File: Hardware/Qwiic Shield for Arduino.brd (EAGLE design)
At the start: 53.3 x 59.7 mm, 25 parts, among them J1 Qwiic Right Angle, J10 Qwiic Right Angle, J8 Qwiic Right Angle, J9 Qwiic Right Angle, Q1 BSS138, Q2 BSS138, U1 ARDUINO UNO

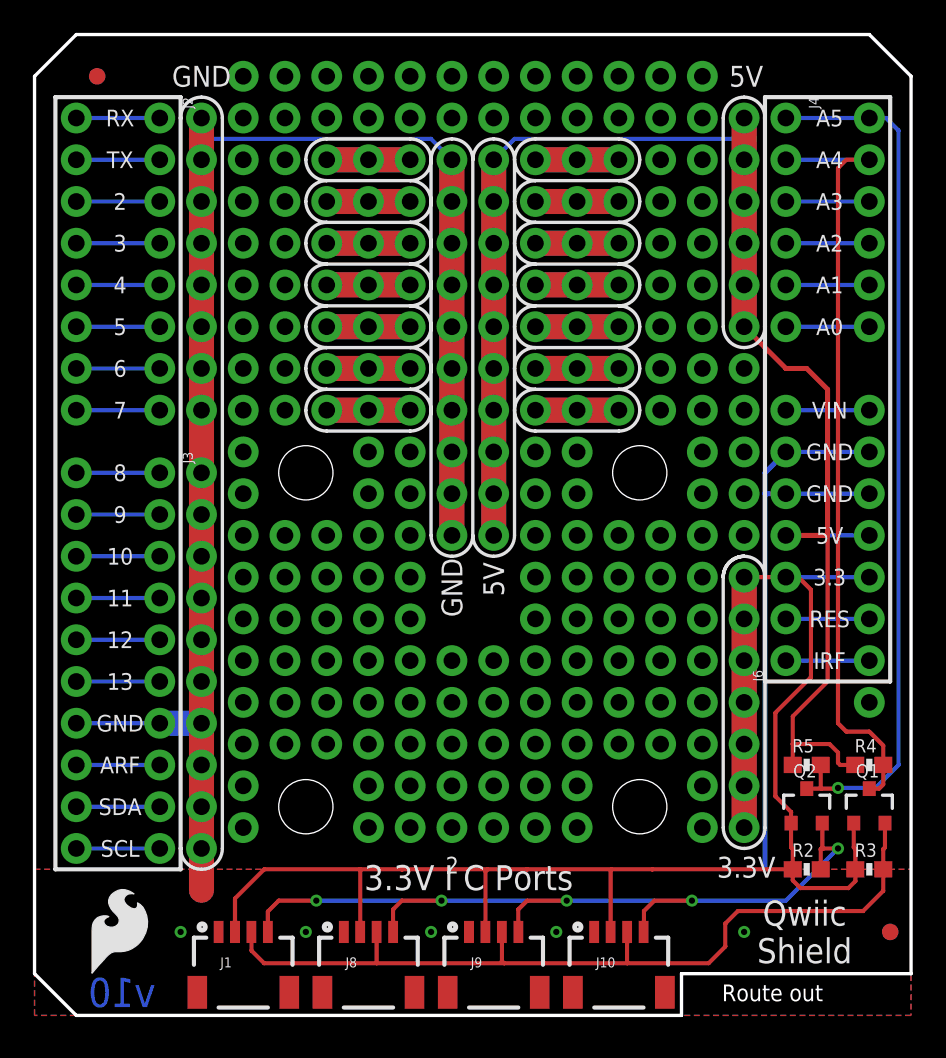
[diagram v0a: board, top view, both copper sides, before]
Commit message: Connected R3 SDA/SCL pins and IOREF
-SDA and SCL are now connected to both A4 /A5 pins and SDA/SCL pins.
-Changed "high" logic side of converters to IOREF, to allow the Arduino to supply it's own IOREF. This will allow the shield to work with 3.3V logic Arduinos.
-named PTH headers in the row of 3.3V to avoid overlap DRC errors.
bumped version to v11 insch and brd
- Added I2C pullup jumper to bottom side with label
- rerouted SDA/SCL to allow for better GND return in pour
- bumped up 3.3V traces to 0.020 inch for qwiic connectors
- all labels to buzzrds and included qwiic logo
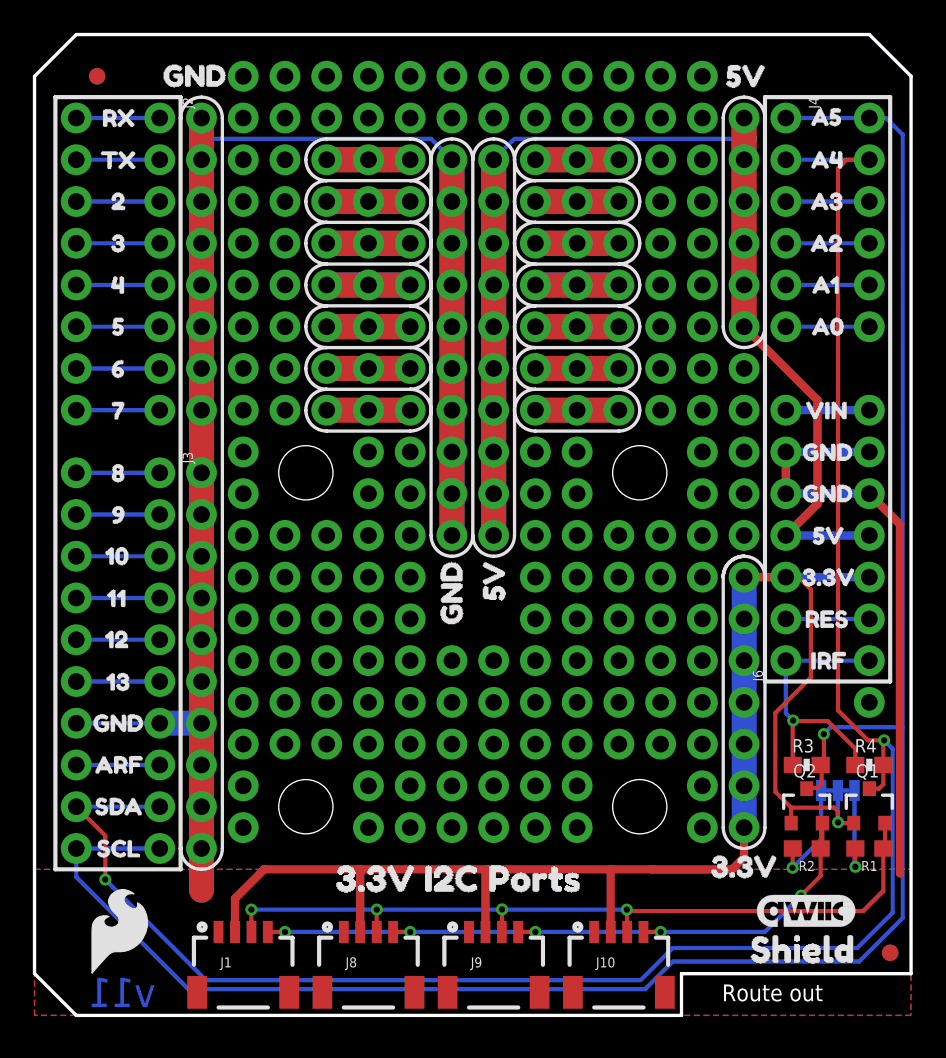
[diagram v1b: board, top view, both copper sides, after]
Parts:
- removed R5: 4.7K, SparkFun-Resistors:0603-RES
- added I2C: (no value), SparkFun-Jumpers:SMT-JUMPER_3_2-NC_TRACE_SILK
- added LOGO3, LOGO4: QWIIC_LOGO_6MM, SparkFun-Aesthetics:QWIIC_6MM
- added R1: 4.7k, SparkFun-Resistors:0603
- added U$10, U$9: (no value), buzzard_labels:TX6
- added U$11, U$12: (no value), buzzard_labels:27
- added U$13, U$14: (no value), buzzard_labels:38
- added U$15, U$16: (no value), buzzard_labels:49
- added U$17, U$18: (no value), buzzard_labels:510
- added U$19, U$20: (no value), buzzard_labels:611
- added U$21, U$23: (no value), buzzard_labels:712
- added U$22: (no value), buzzard_labels (3):I2C0
- added U$24, U$25: (no value), buzzard_labels:813
- added U$26, U$27: (no value), buzzard_labels:914
- added U$28, U$29: (no value), buzzard_labels:1015
- added U$30, U$31: (no value), buzzard_labels:1116
- added U$32, U$33: (no value), buzzard_labels:1217
- added U$34, U$35: (no value), buzzard_labels:1318
- added U$36, U$37, U$68, U$69, U$70, U$71: (no value), buzzard_labels:GND30
- added U$38, U$39: (no value), buzzard_labels:ARF20
- added U$4, U$5: (no value), buzzard_labels:SHIELD0
- added U$40, U$41: (no value), buzzard_labels:SDA21
- added U$42, U$43: (no value), buzzard_labels:SCL22
- added U$44, U$45, U$46, U$47: (no value), buzzard_labels:GND2
- added U$48, U$49: (no value), buzzard_labels:3#3V4
- added U$50, U$51, U$52, U$53: (no value), buzzard_labels:5V3
- added U$54, U$55: (no value), buzzard_labels:A523
- added U$56, U$57: (no value), buzzard_labels:A424
- added U$58, U$59: (no value), buzzard_labels:A325
- added U$6: (no value), buzzard_labels:3#3V_I2C_PORTS1
- added U$60, U$61: (no value), buzzard_labels:A226
- added U$62, U$63: (no value), buzzard_labels:A127
- added U$64, U$65: (no value), buzzard_labels:A028
- added U$66, U$67: (no value), buzzard_labels:VIN29
- added U$7, U$8: (no value), buzzard_labels:RX5
- added U$72, U$73: (no value), buzzard_labels:5V31
- added U$74, U$75: (no value), buzzard_labels:3#3V32
- added U$76, U$77: (no value), buzzard_labels:RES33
- added U$78, U$79: (no value), buzzard_labels:IRF34
- R2: value 4.7K -> 4.7k; device SparkFun-Resistors:0603-RES -> SparkFun-Resistors:0603
- moved LOGO1 42.1 mm to (5.08, 5.08)
- moved R3 7.41 mm to (47.0, 15.2)
- moved FD1 1.27 mm to (52.1, 3.81)
- moved FD3 1.27 mm to (52.1, 3.81)
- moved R2 1.27 mm to (47.0, 10.2), turned to 180 degrees
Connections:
- removed net HV_SCL: J4.1, Q2.3, R5.2, U1.A5
- removed net HV_SDA: J4.2, Q1.3, R4.2, U1.A4
- removed net SCL1: J3.10, U1.SCL
- removed net SDA1: J3.9, U1.SDA
- new net N$76: I2C.3, R1.2
- new net N$78: I2C.1, R2.2
- new net SCL_R3: J3.10, J4.1, Q2.3, R3.2, U1.A5, U1.SCL
- new net SDA_R3: J3.9, J4.2, Q1.3, R4.2, U1.A4, U1.SDA
- net 3.3V: now also I2C.2; no longer R2.1, R3.1
- net 5V: no longer R4.1, R5.1
- net IOREF: now also R3.1, R4.1
- net SCL: now also R2.1; no longer R2.2
- net SDA: now also R1.1; no longer R3.2
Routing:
- net SCL_R3: track 0.00 -> 126.1 mm, vias 0 -> 1
- net SDA_R3: track 0.00 -> 120.5 mm, vias 0 -> 2
- net HV_SCL: track 53.4 -> 0.00 mm, vias 1 -> 0
- net HV_SDA: track 47.6 -> 0.00 mm
- net 5V: track 129.6 -> 107.3 mm
- net 3.3V: track 115.0 -> 94.1 mm, vias 2 -> 8
- net SCL: track 54.9 -> 41.4 mm
- net IOREF: track 5.08 -> 17.1 mm, vias 0 -> 1
- net N$78: track 0.00 -> 6.62 mm
- net N$76: track 0.00 -> 5.79 mm, vias 0 -> 1
- net SDA1: track 5.08 -> 0.00 mm
- net SCL1: track 5.08 -> 0.00 mm
- net SDA: track 52.5 -> 48.6 mm, vias 0 -> 4
- net GND: track 201.4 -> 200.0 mm, vias 33 -> 28
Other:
- board text added: "A. England, P. Lewis"
- board text added: "v11"
- board text removed: "10"
- board text removed: "11"
- board text removed: "12"
- board text removed: "13"
- board text removed: "2"
- board text removed: "3"
- board text removed: "3.3"
- board text removed: "3.3V"
- board text removed: "3.3V I C Ports"
- board text removed: "4"
- board text removed: "5"
- board text removed: "5V"
- board text removed: "6"
- board text removed: "7"
- board text removed: "8"
- board text removed: "9"
- board text removed: "A. England"
- board text removed: "A0"
- board text removed: "A1"
- board text removed: "A2"
- board text removed: "A3"
- board text removed: "A4"
- board text removed: "A5"
- board text removed: "ARF"
- board text removed: "GND"
- board text removed: "IRF"
- board text removed: "Qwiic Shield"
- board text removed: "RES"
- board text removed: "RX"
- board text removed: "SCL"
- board text removed: "SDA"
- board text removed: "TX"
- board text removed: "VIN"
- board text removed: "v10"

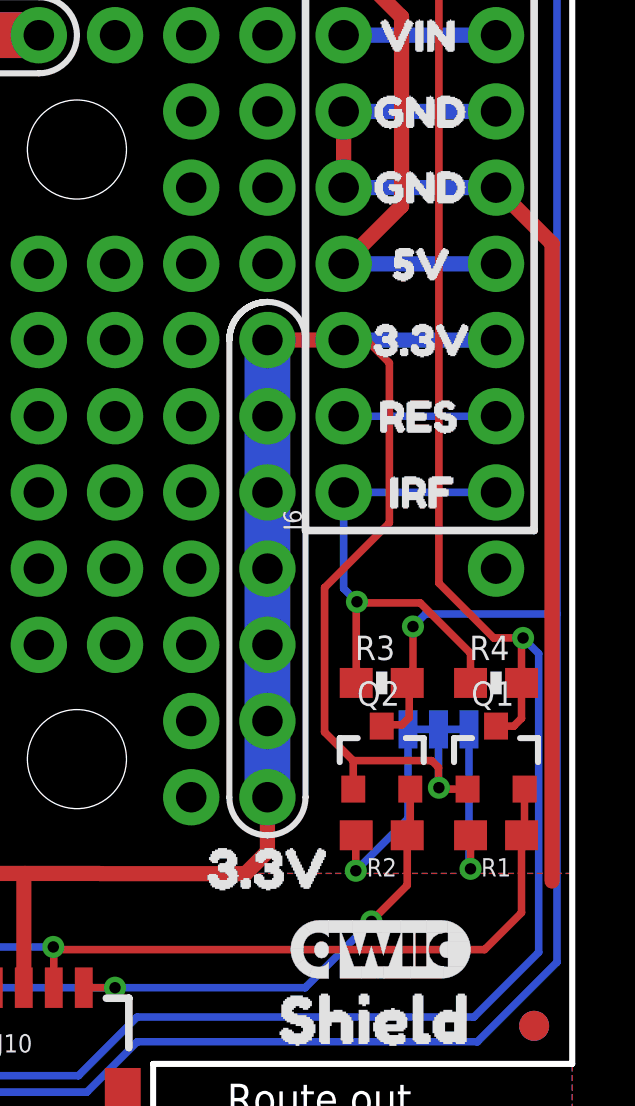
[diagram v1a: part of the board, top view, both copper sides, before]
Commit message: Moved resistors to original location to maintain stencil spacing
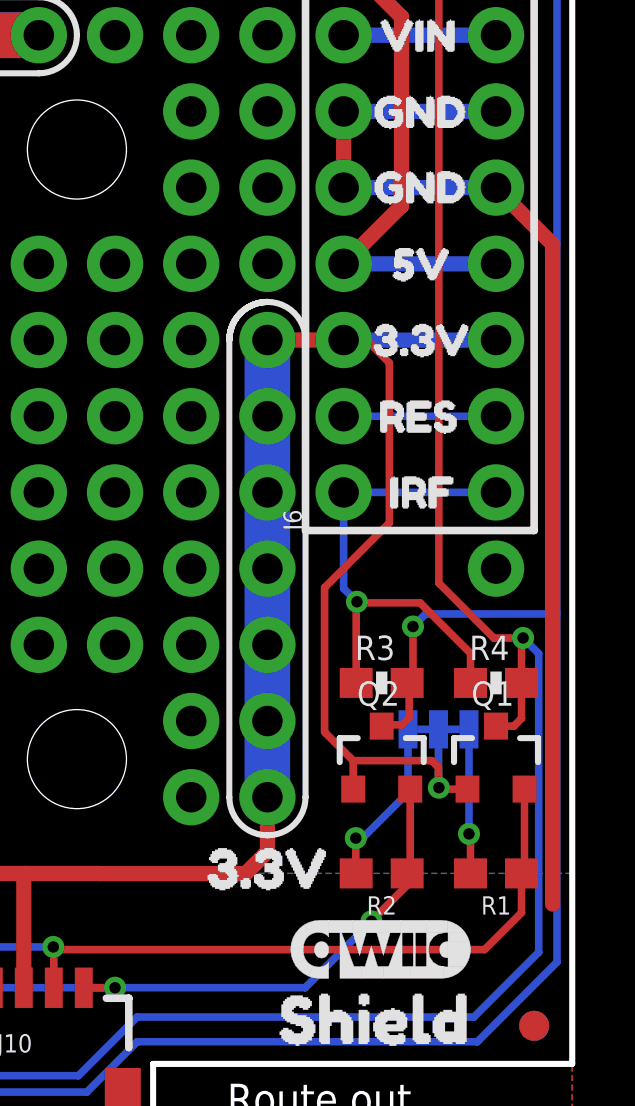
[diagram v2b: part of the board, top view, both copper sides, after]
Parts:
- moved R1 1.27 mm to (50.8, 8.89)
- moved R2 1.27 mm to (47.0, 8.89)
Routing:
- net N$76: track 5.79 -> 4.82 mm
- net N$78: track 6.62 -> 5.66 mm
- net GND: track 200.0 -> 200.8 mm
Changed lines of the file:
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@@
 <setting verticaltext="up"/>
 </settings>
-<grid distance="0.05" unitdist="inch" unit="inch" style="lines" multiple="1" display="yes" altdistance="0.0005" altunitdist="inch" altunit="inch"/>
+<grid distance="0.05" unitdist="inch" unit="inch" style="lines" multiple="1" display="yes" altdistance="0.0001" altunitdist="inch" altunit="inch"/>
 <layers>
 <layer number="1" name="Top" color="4" fill="1" visible="yes" active="yes"/>
@@
 <element name="FD4" library="SparkFun-Aesthetics" package="FIDUCIAL-1X2" value="FIDUCIAL1X2" x="3.81" y="57.15" smashed="yes" rot="MR0"/>
 <element name="U$1" library="SparkFun-Aesthetics" package="SFE_LOGO_FLAME_.2" value="" x="3.1496" y="2.2987" smashed="yes"/>
-<element name="R1" library="SparkFun-Resistors" package="0603" value="4.7k" x="50.8" y="10.16" smashed="yes" rot="R180">
-<attribute name="NAME" x="50.8" y="9.398" size="0.6096" layer="25" font="vector" ratio="20" rot="R180" align="bottom-center"/>
-<attribute name="PROD_ID" value="RES-07857" x="49.53" y="10.16" size="1.778" layer="27" rot="R180" display="off"/>
-<attribute name="VALUE" x="50.8" y="10.922" size="0.6096" layer="27" font="vector" ratio="20" rot="R180" align="top-center"/>
+<element name="R1" library="SparkFun-Resistors" package="0603" value="4.7k" x="50.8" y="8.89" smashed="yes" rot="R180">
+<attribute name="NAME" x="50.8" y="8.128" size="0.6096" layer="25" font="vector" ratio="20" rot="R180" align="bottom-center"/>
+<attribute name="PROD_ID" value="RES-07857" x="49.53" y="8.89" size="1.778" layer="27" rot="R180" display="off"/>
+<attribute name="VALUE" x="50.8" y="9.652" size="0.6096" layer="27" font="vector" ratio="20" rot="R180" align="top-center"/>
 </element>
-<element name="R2" library="SparkFun-Resistors" package="0603" value="4.7k" x="46.99" y="10.16" smashed="yes" rot="R180">
-<attribute name="NAME" x="46.99" y="9.398" size="0.6096" layer="25" font="vector" ratio="20" rot="R180" align="bottom-center"/>
-<attribute name="PROD_ID" value="RES-07857" x="45.72" y="10.16" size="1.778" layer="27" rot="R180" display="off"/>
-<attribute name="VALUE" x="46.99" y="10.922" size="0.6096" layer="27" font="vector" ratio="20" rot="R180" align="top-center"/>
+<element name="R2" library="SparkFun-Resistors" package="0603" value="4.7k" x="46.99" y="8.89" smashed="yes" rot="R180">
+<attribute name="NAME" x="46.99" y="8.128" size="0.6096" layer="25" font="vector" ratio="20" rot="R180" align="bottom-center"/>
+<attribute name="PROD_ID" value="RES-07857" x="45.72" y="8.89" size="1.778" layer="27" rot="R180" display="off"/>
+<attribute name="VALUE" x="46.99" y="9.652" size="0.6096" layer="27" font="vector" ratio="20" rot="R180" align="top-center"/>
 </element>
 <element name="I2C" library="SparkFun-Jumpers" package="SMT-JUMPER_3_2-NC_TRACE_SILK" value="" x="48.8823" y="13.6906" smashed="yes" rot="MR180">
@@
 <wire x1="24.13" y1="53.34" x2="10.16" y2="53.34" width="0.254" layer="16"/>
 <wire x1="45.72" y1="34.29" x2="45.72" y2="31.75" width="0.508" layer="1"/>
-<wire x1="50.8" y1="31.75" x2="52.6669" y2="29.8831" width="0.508" layer="1"/>
-<wire x1="52.6669" y1="29.8831" x2="52.6669" y2="8.636" width="0.508" layer="1"/>
+<wire x1="50.8" y1="31.75" x2="52.687221875" y2="29.862778125" width="0.508" layer="1"/>
+<wire x1="52.687221875" y1="29.862778125" x2="52.687221875" y2="7.863840625" width="0.508" layer="1"/>
 </signal>
 <signal name="3.3V">
@@
 <wire x1="37.084" y1="5.104" x2="37.06" y2="5.08" width="0.254" layer="1"/>
 <contactref element="R2" pad="1"/>
-<wire x1="47.94" y1="11.7" x2="47.94" y2="10.26" width="0.254" layer="1"/>
-<wire x1="47.94" y1="10.26" x2="47.84" y2="10.16" width="0.254" layer="1"/>
-<wire x1="47.84" y1="10.16" x2="47.84" y2="8.4954" width="0.254" layer="1"/>
+<wire x1="47.94" y1="11.7" x2="47.94" y2="8.99" width="0.254" layer="1"/>
+<wire x1="47.94" y1="8.99" x2="47.84" y2="8.89" width="0.254" layer="1"/>
+<wire x1="47.84" y1="8.89" x2="47.84" y2="8.4954" width="0.254" layer="1"/>
 <wire x1="14.2" y1="5.08" x2="15.24" y2="5.08" width="0.254" layer="1"/>
 <via x="15.24" y="5.08" extent="1-16" drill="0.381"/>
@@
 <wire x1="50.419" y1="6.35" x2="51.65" y2="7.581" width="0.254" layer="1"/>
 <contactref element="R1" pad="1"/>
-<wire x1="51.65" y1="7.581" x2="51.65" y2="10.16" width="0.254" layer="1"/>
-<wire x1="51.65" y1="10.16" x2="51.75" y2="10.26" width="0.254" layer="1"/>
-<wire x1="51.75" y1="10.26" x2="51.75" y2="11.7" width="0.254" layer="1"/>
+<wire x1="51.65" y1="7.581" x2="51.65" y2="8.89" width="0.254" layer="1"/>
+<wire x1="51.65" y1="8.89" x2="51.75" y2="8.99" width="0.254" layer="1"/>
+<wire x1="51.75" y1="8.99" x2="51.75" y2="11.7" width="0.254" layer="1"/>
 <wire x1="36.06" y1="5.08" x2="36.06" y2="6.4215" width="0.254" layer="1"/>
 <wire x1="36.06" y1="6.4215" x2="36.0426" y2="6.4389" width="0.254" layer="1"/>
@@
 <contactref element="R1" pad="2"/>
 <contactref element="I2C" pad="3"/>
-<wire x1="49.95" y1="10.16" x2="49.95" y2="9.0433" width="0.254" layer="1"/>
-<wire x1="49.95" y1="9.0433" x2="49.9491" y2="9.0424" width="0.254" layer="1"/>
-<via x="49.9491" y="9.0424" extent="1-16" drill="0.381"/>
-<wire x1="49.9491" y1="9.0424" x2="49.8983" y2="9.0932" width="0.254" layer="16"/>
-<wire x1="49.8983" y1="9.0932" x2="49.8983" y2="13.6906" width="0.254" layer="16"/>
+<wire x1="49.8983" y1="10.2082625" x2="49.95" y2="10.1565625" width="0.254" layer="1"/>
+<wire x1="49.95" y1="10.1565625" x2="49.95" y2="8.89" width="0.254" layer="1"/>
+<via x="49.8983" y="10.2082625" extent="1-16" drill="0.381"/>
+<wire x1="49.8983" y1="10.2082625" x2="49.8983" y2="13.6906" width="0.254" layer="16"/>
 </signal>
 <signal name="N$78">
 <contactref element="R2" pad="2"/>
 <contactref element="I2C" pad="1"/>
-<wire x1="47.8663" y1="13.6906" x2="47.8663" y2="10.7188" width="0.254" layer="16"/>
-<wire x1="47.8663" y1="10.7188" x2="46.1264" y2="8.9789" width="0.254" layer="16"/>
-<via x="46.1264" y="8.9789" extent="1-16" drill="0.381"/>
-<wire x1="46.1264" y1="8.9789" x2="46.1264" y2="10.1464" width="0.254" layer="1"/>
-<wire x1="46.1264" y1="10.1464" x2="46.14" y2="10.16" width="0.254" layer="1"/>
+<wire x1="47.8663" y1="13.6906" x2="47.8663" y2="11.5824" width="0.254" layer="16"/>
+<wire x1="47.8663" y1="11.5824" x2="46.349921875" y2="10.066021875" width="0.254" layer="16"/>
+<wire x1="46.349921875" y1="10.066021875" x2="46.1264" y2="10.066021875" width="0.254" layer="16"/>
+<via x="46.1264" y="10.066021875" extent="1-16" drill="0.381"/>
+<wire x1="46.1264" y1="10.066021875" x2="46.1264" y2="8.9036" width="0.254" layer="1"/>
+<wire x1="46.14" y1="8.89" x2="46.1264" y2="8.9036" width="0.254" layer="1"/>
 </signal>
 </signals>

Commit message: Moved qwiic board to SFE library
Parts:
- U$3: device SparkX:QWIIC_BOARD_MOUNT_HOLES -> SparkFun-Boards:QWIIC_BOARD_MOUNT_HOLES
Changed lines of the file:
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@@
 </element>
 <element name="U$2" library="SparkFun-Aesthetics" package="SFE_LOGO_NAME_FLAME_.1" value="SFE_LOGO_NAME_FLAME.1_INCH" x="33.02" y="1.27" smashed="yes" rot="MR0"/>
-<element name="U$3" library="SparkX" package="QWIIC_BOARD_MOUNT_HOLES" value="QWIIC_BOARD_OUTLINEH" x="26.67" y="22.86" smashed="yes" rot="R90"/>
+<element name="U$3" library="SparkFun-Boards" package="QWIIC_BOARD_MOUNT_HOLES" value="QWIIC_BOARD_OUTLINEH" x="26.67" y="22.86" smashed="yes" rot="R90"/>
 <element name="LOGO2" library="SparkFun-Aesthetics" package="REVISION" value="REVISION" x="2.54" y="-30.48" smashed="yes"/>
 <element name="FD3" library="SparkFun-Aesthetics" package="FIDUCIAL-1X2" value="FIDUCIAL1X2" x="52.07" y="3.81" smashed="yes" rot="MR0"/>
